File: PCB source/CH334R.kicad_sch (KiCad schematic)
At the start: 6 parts, among them U4 CH334R, Y4 12MHz

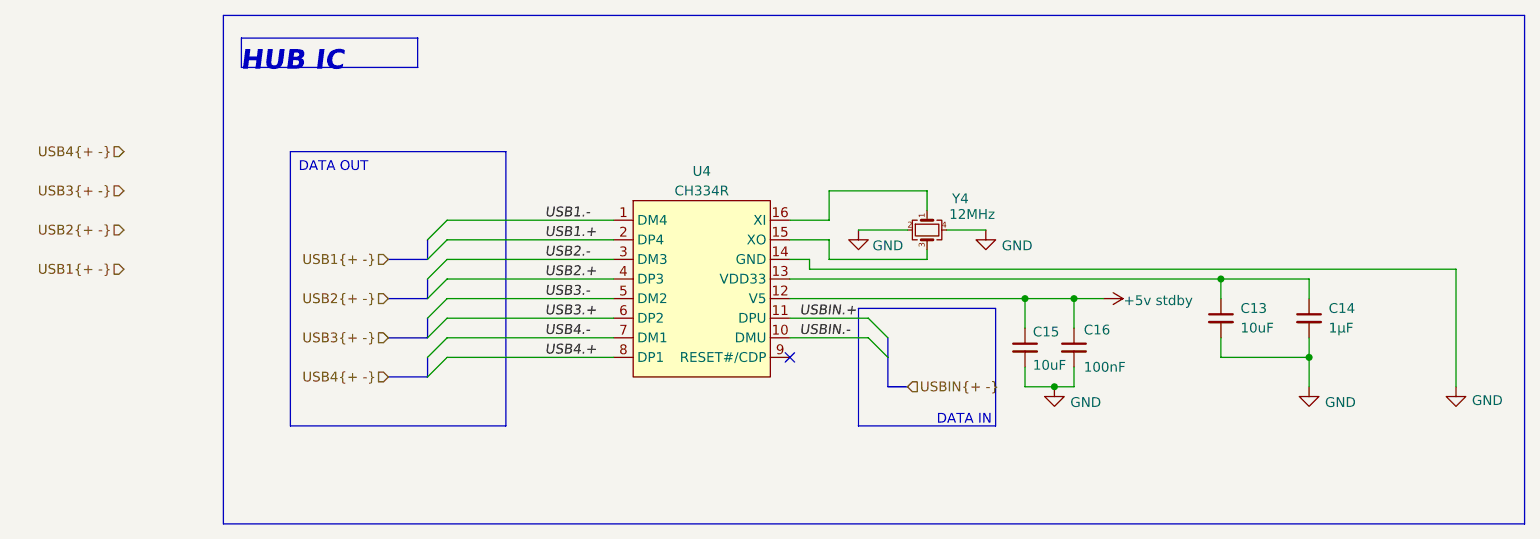
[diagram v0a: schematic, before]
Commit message: change USB upstream pinout
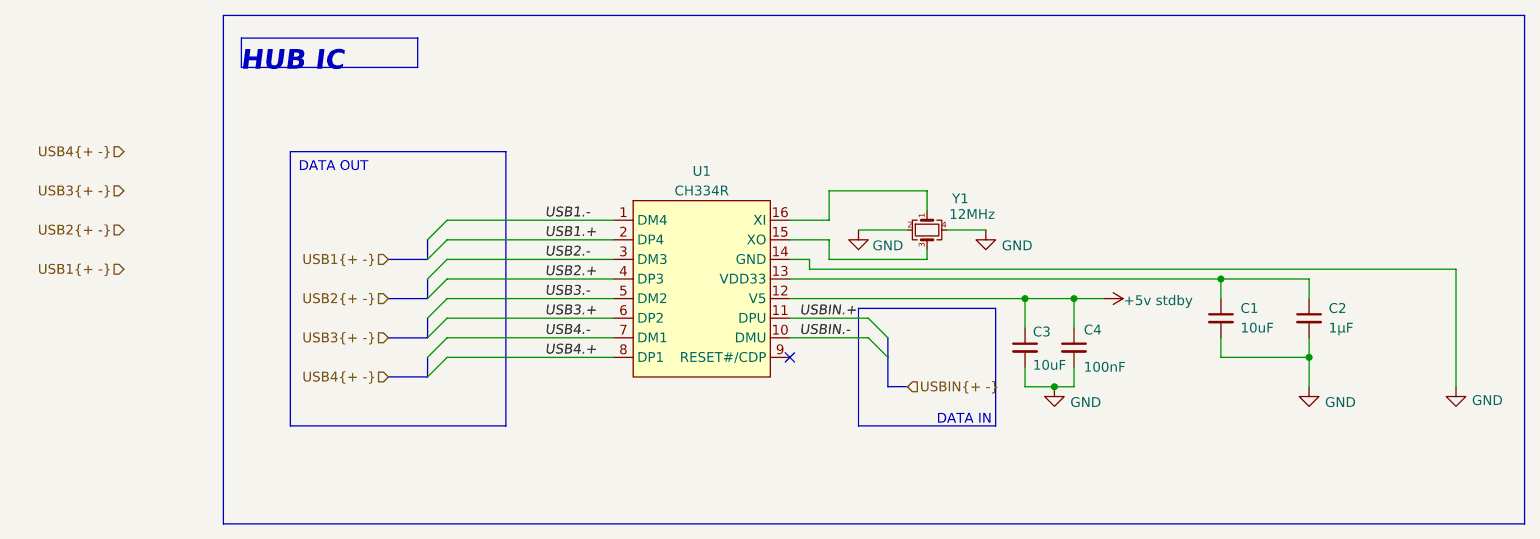
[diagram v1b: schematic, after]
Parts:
- renumbered C13 to C1, C14 to C2, C15 to C3, C16 to C4, U4 to U1, Y4 to Y1
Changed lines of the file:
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@@
 (kicad_sch
-	(version 20231120)
+	(version 20250114)
 	(generator "eeschema")
-	(generator_version "8.0")
+	(generator_version "9.0")
 	(paper "A4")
 	(title_block
@@
 		(comment 1 "Artem Horiunov")
 	)
+	(rectangle
+		(start 76.2 76.2)
+		(end 104.14 111.76)
+		(stroke
+			(width 0.127)
+			(type default)
+		)
+		(fill
+			(type none)
+		)
+	)
+	(rectangle
+		(start 149.86 96.52)
+		(end 167.64 111.76)
+		(stroke
+			(width 0.127)
+			(type default)
+		)
+		(fill
+			(type none)
+		)
+	)
+	(rectangle
+		(start 67.5148 58.5348)
+		(end 236.22 124.46)
+		(stroke
+			(width 0)
+			(type default)
+		)
+		(fill
+			(type none)
+		)
+	)
+	(rectangle
+		(start 88.9 53.34)
+		(end 88.9 53.34)
+		(stroke
+			(width 0)
+			(type default)
+		)
+		(fill
+			(type none)
+		)
+	)
+	(rectangle
+		(start 69.85 61.468)
+		(end 92.71 65.278)
+		(stroke
+			(width 0)
+			(type default)
+		)
+		(fill
+			(type none)
+		)
+	)
+	(text "DATA OUT\n"
+		(exclude_from_sim no)
+		(at 81.788 78.232 0)
+		(effects
+			(font
+				(size 1.27 1.27)
+			)
+		)
+	)
+	(text "DATA IN\n"
+		(exclude_from_sim no)
+		(at 163.576 110.998 0)
+		(effects
+			(font
+				(size 1.27 1.27)
+			)
+		)
+	)
+	(text "HUB IC\n"
+		(exclude_from_sim no)
+		(at 76.454 64.516 0)
+		(effects
+			(font
+				(size 2.54 2.54)
+				(thickness 0.254)
+				(bold yes)
+				(italic yes)
+			)
+		)
+	)
 	(junction
 		(at 196.85 92.71)
@@
 		)
 	)
-	(rectangle
-		(start 76.2 76.2)
-		(end 104.14 111.76)
-		(stroke
-			(width 0.127)
-			(type default)
-		)
-		(fill
-			(type none)
-		)
-	)
-	(rectangle
-		(start 149.86 96.52)
-		(end 167.64 111.76)
-		(stroke
-			(width 0.127)
-			(type default)
-		)
-		(fill
-			(type none)
-		)
-	)
-	(rectangle
-		(start 67.5148 58.5348)
-		(end 236.22 124.46)
-		(stroke
-			(width 0)
-			(type default)
-		)
-		(fill
-			(type none)
-		)
-	)
-	(rectangle
-		(start 88.9 53.34)
-		(end 88.9 53.34)
-		(stroke
-			(width 0)
-			(type default)
-		)
-		(fill
-			(type none)
-		)
-	)
-	(rectangle
-		(start 69.85 61.468)
-		(end 92.71 65.278)
-		(stroke
-			(width 0)
-			(type default)
-		)
-		(fill
-			(type none)
-		)
-	)
-	(text "DATA OUT\n"
-		(exclude_from_sim no)
-		(at 81.788 78.232 0)
-		(effects
-			(font
-				(size 1.27 1.27)
-			)
-		)
-	)
-	(text "DATA IN\n"
-		(exclude_from_sim no)
-		(at 163.576 110.998 0)
-		(effects
-			(font
-				(size 1.27 1.27)
-			)
-		)
-	)
-	(text "HUB IC\n"
-		(exclude_from_sim no)
-		(at 76.454 64.516 0)
-		(effects
-			(font
-				(size 2.54 2.54)
-				(thickness 0.254)
-				(bold yes)
-				(italic yes)
-			)
-		)
-	)
 	(label "USB4.+"
 		(at 109.22 102.87 0)
-		(fields_autoplaced yes)
 		(effects
 			(font
@@
 	(label "USBIN.-"
 		(at 142.24 100.33 0)
-		(fields_autoplaced yes)
 		(effects
 			(font
@@
 	(label "USB3.+"
 		(at 109.22 97.79 0)
-		(fields_autoplaced yes)
 		(effects
 			(font
@@
 	(label "USBIN.+"
 		(at 142.24 97.79 0)
-		(fields_autoplaced yes)
 		(effects
 			(font
@@
 	(label "USB1.+"
 		(at 109.22 87.63 0)
-		(fields_autoplaced yes)
 		(effects
 			(font
@@
 	(label "USB3.-"
 		(at 109.22 95.25 0)
-		(fields_autoplaced yes)
 		(effects
 			(font
@@
 	(label "USB2.-"
 		(at 109.22 90.17 0)
-		(fields_autoplaced yes)
 		(effects
 			(font
@@
 	(label "USB2.+"
 		(at 109.22 92.71 0)
-		(fields_autoplaced yes)
 		(effects
 			(font
@@
 	(label "USB1.-"
 		(at 109.22 85.09 0)
-		(fields_autoplaced yes)
 		(effects
 			(font
@@
 	(label "USB4.-"
 		(at 109.22 100.33 0)
-		(fields_autoplaced yes)
 		(effects
 			(font
@@
 		(shape input)
 		(at 54.61 91.44 180)
-		(fields_autoplaced yes)
 		(effects
 			(font
@@
 		(shape input)
 		(at 88.9 105.41 180)
-		(fields_autoplaced yes)
 		(effects
 			(font
@@
 		(shape input)
 		(at 54.61 86.36 180)
-		(fields_autoplaced yes)
 		(effects
 			(font
@@
 		(shape input)
 		(at 88.9 95.25 180)
-		(fields_autoplaced yes)
 		(effects
 			(font
@@
 		(shape input)
 		(at 156.21 106.68 0)
-		(fields_autoplaced yes)
 		(effects
 			(font
@@
 		(shape input)
 		(at 54.61 81.28 180)
-		(fields_autoplaced yes)
 		(effects
 			(font
@@
 		(shape input)
 		(at 54.61 76.2 180)
-		(fields_autoplaced yes)
 		(effects
 			(font
@@
 		(shape input)
 		(at 88.9 90.17 180)
-		(fields_autoplaced yes)
 		(effects
 			(font
@@
 		(shape input)
 		(at 88.9 100.33 180)
-		(fields_autoplaced yes)
 		(effects
 			(font
@@
 		(on_board yes)
 		(dnp no)
-		(property "Reference" "#PWR0269"
+		(property "Reference" "#PWR045"
 			(at 208.28 113.03 0)
 			(effects
@@
 		(on_board yes)
 		(dnp no)
-		(property "Reference" "Y4"
+		(property "Reference" "Y1"
 			(at 163.068 82.296 90)
 			(effects
@@
 		(on_board yes)
 		(dnp no)
-		(property "Reference" "#PWR0268"
+		(property "Reference" "#PWR044"
 			(at 175.26 113.03 0)
 			(effects
@@
 		(on_board yes)
 		(dnp no)
-		(property "Reference" "U4"
+		(property "Reference" "U1"
 			(at 129.54 78.74 0)
 			(effects
@@
 		(on_board yes)
 		(dnp no)
-		(property "Reference" "#PWR0267"
+		(property "Reference" "#PWR043"
 			(at 177.8 95.25 0)
 			(effects
@@
 		(on_board yes)
 		(dnp no)
-		(property "Reference" "#PWR0266"
+		(property "Reference" "#PWR042"
 			(at 166.37 92.71 0)
 			(effects
@@
 		(on_board yes)
 		(dnp no)
-		(property "Reference" "C14"
+		(property "Reference" "C2"
 			(at 210.82 96.52 0)
 			(effects
@@
 		(on_board yes)
 		(dnp no)
-		(property "Reference" "C16"
+		(property "Reference" "C4"
 			(at 179.07 99.314 0)
 			(effects
@@
 		(on_board yes)
 		(dnp no)
-		(property "Reference" "#PWR0270"
+		(property "Reference" "#PWR046"
 			(at 227.33 113.03 0)
 			(effects
@@
 		(on_board yes)
 		(dnp no)
-		(property "Reference" "#PWR0265"
+		(property "Reference" "#PWR041"
 			(at 149.86 92.71 0)
 			(effects
@@
 		(on_board yes)
 		(dnp no)
-		(property "Reference" "C13"
+		(property "Reference" "C1"
 			(at 199.39 96.52 0)
 			(effects
@@
 		(on_board yes)
 		(dnp no)
-		(property "Reference" "C15"
+		(property "Reference" "C3"
 			(at 172.466 99.568 0)
 			(effects
